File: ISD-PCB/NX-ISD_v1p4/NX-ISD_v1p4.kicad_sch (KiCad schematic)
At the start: 1 part

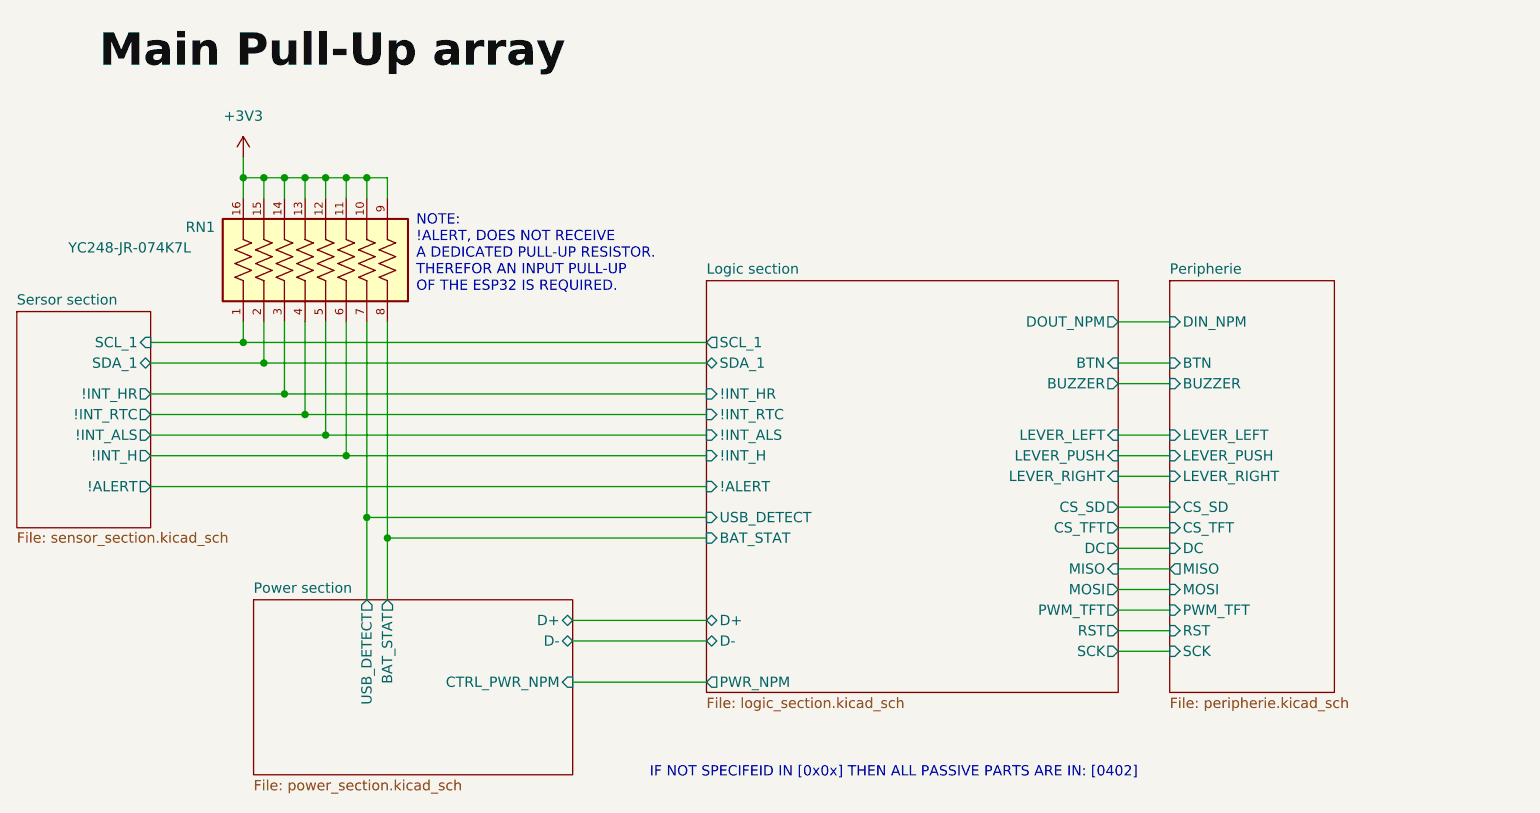
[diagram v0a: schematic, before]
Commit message: feat(pcb): v1.4 schematic and layout updates for 4-bit SDMMC, direct display SPI, and button pullups
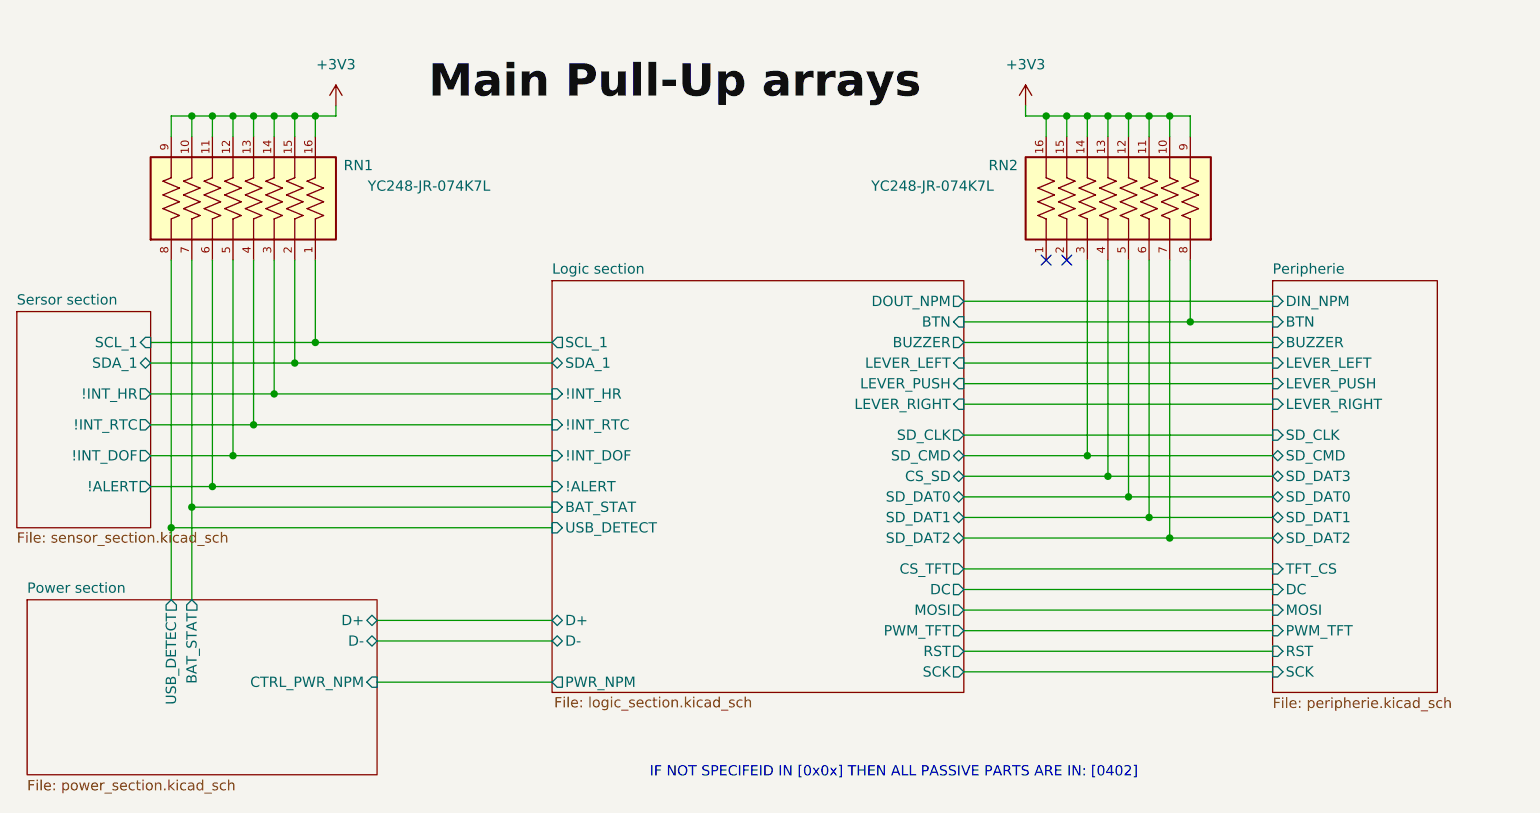
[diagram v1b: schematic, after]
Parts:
- added RN2: YC248-JR-074K7L, NX-AW-footprints:RESCAXS50P400X160X55-16N, symbol YC248-JR-074K7L:YC248-JR-074K7L
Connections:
- net Logic section/!INT_H is gone; now on net Logic section/!ALERT: RN1.6
- net +3V3: now also RN2.10, RN2.11, RN2.12, RN2.13, RN2.14, RN2.15, RN2.16, RN2.9
- net Logic section/BAT_STAT: now also RN1.7; no longer RN1.8
- net Logic section/BTN: now also RN2.8
- net Logic section/CS_SD: now also RN2.4
- net Logic section/USB_DETECT: now also RN1.8; no longer RN1.7
- net Logic section/!INT_ALS renamed Logic section/!INT_DOF
- new net Logic section/SD_CMD: RN2.3
- new net Logic section/SD_DAT0: RN2.5
- new net Logic section/SD_DAT1: RN2.6
- new net Logic section/SD_DAT2: RN2.7
- no-connect marks 0 -> 2
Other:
- sheet Logic section ports: added !INT_DOF, SD_CLK, SD_CMD, SD_DAT0, SD_DAT1, SD_DAT2; removed !INT_ALS, !INT_H, MISO
- sheet Peripherie ports: added SD_CLK, SD_CMD, SD_DAT0, SD_DAT1, SD_DAT2, SD_DAT3, TFT_CS; removed CS_SD, CS_TFT, MISO
- sheet Sersor section ports: added !INT_DOF; removed !INT_ALS, !INT_H
- note removed: "NOTE: !ALERT, DOES NOT RECEIVE A DEDICATED PULL-UP RESISTOR. THEREFOR AN INPUT PULL-UP OF THE ESP32 IS REQUIRED."

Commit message: hw(v1.4): relocate MicroSD to right edge and re-route BNO085 cluster; update READMEs
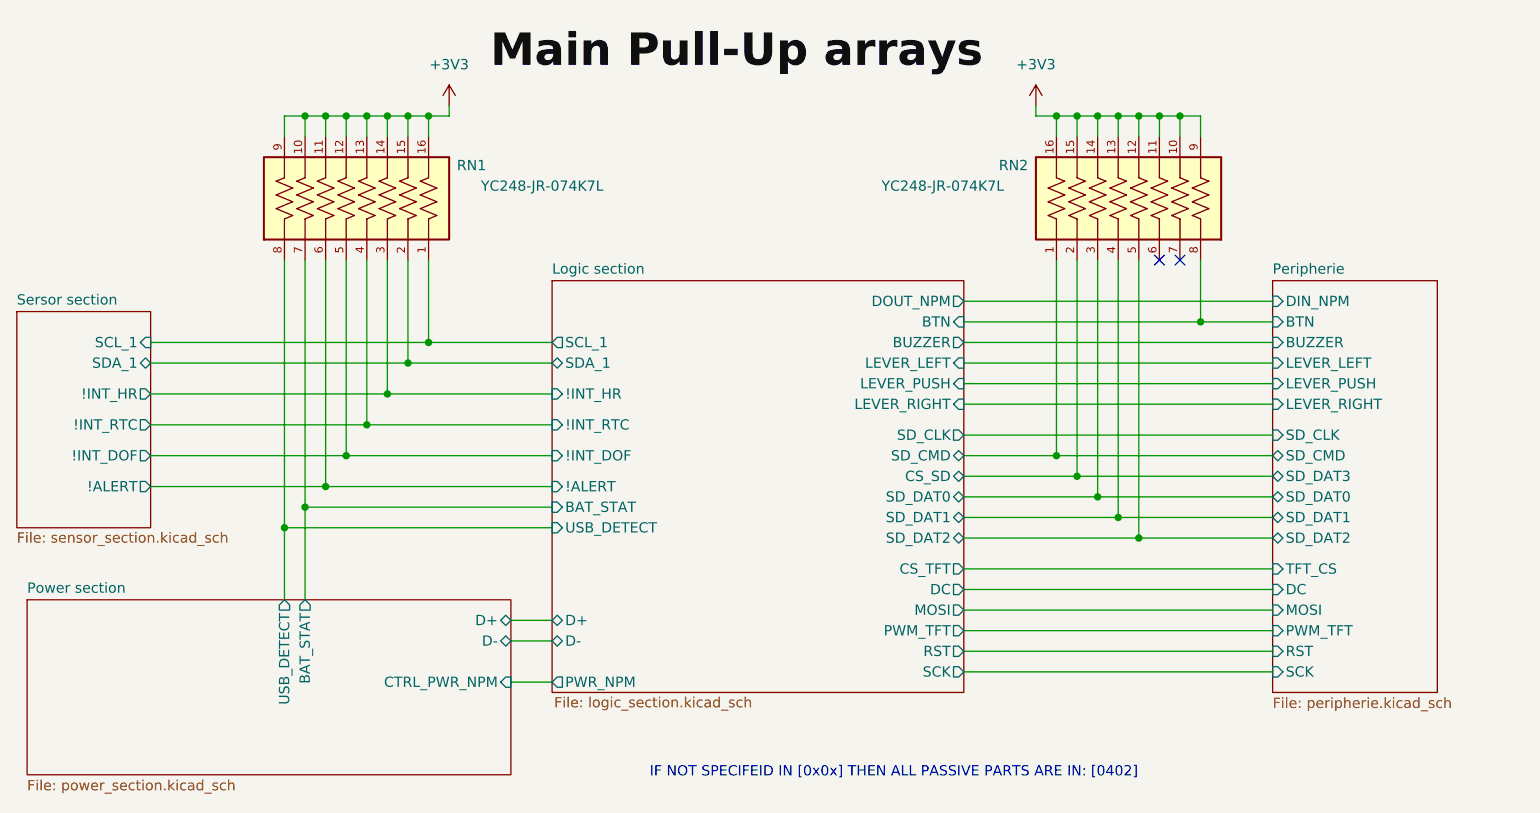
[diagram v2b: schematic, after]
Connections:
- net Logic section/CS_SD: now also RN2.2; no longer RN2.4
- net Logic section/SD_CMD: now also RN2.1; no longer RN2.3
- net Logic section/SD_DAT0: now also RN2.3; no longer RN2.5
- net Logic section/SD_DAT1: now also RN2.4; no longer RN2.6
- net Logic section/SD_DAT2: now also RN2.5; no longer RN2.7
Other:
- moved on the sheet: RN1

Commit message: hw(v1.4): progress on TODO - 4-bit MicroSD, direct display bus, BNO085 & EP vias (DRC 0 errors)
- Implemented 4-bit SDMMC MicroSD slot (Molex 105162-0001) on right edge with outward insertion
- Routed direct 3.3V display SPI bus (TE 1-2328702-0) with C29 100nF decoupling
- Centered BNO085 9-DOF IMU cluster with local ground star and 32.768kHz crystal
- Rerouted NeoPixel PWR_NPM high-side power gate signal
- Updated thermal EP pad via sizes on BQ25170 and MAX17048 for standard JLCPCB fabrication
- Achieved 0 DRC errors, 0 unconnected nets, and 100% schematic parity
- Updated HW-TODO and SW-TODO for v1.3/v1.4 pinout target abstraction
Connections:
- net Logic section/BAT_STAT: now also RN1.8; no longer RN1.7
- net Logic section/SD_CMD: now also RN2.3; no longer RN2.1
- net Logic section/SD_DAT0: now also RN2.4; no longer RN2.3
- net Logic section/SD_DAT1: now also RN2.5; no longer RN2.4
- net Logic section/SD_DAT2: now also RN2.1; no longer RN2.5
- net Logic section/USB_DETECT: now also RN1.7; no longer RN1.8

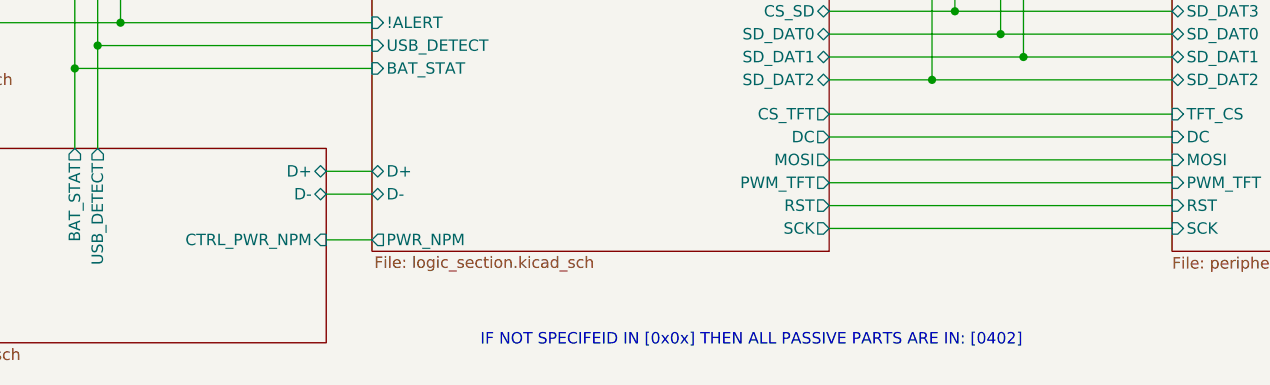
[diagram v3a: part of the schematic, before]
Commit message: hw(v1.4): bq25170 thermal optimization, usb-c plating, battery pad stitching, and npm decoupling
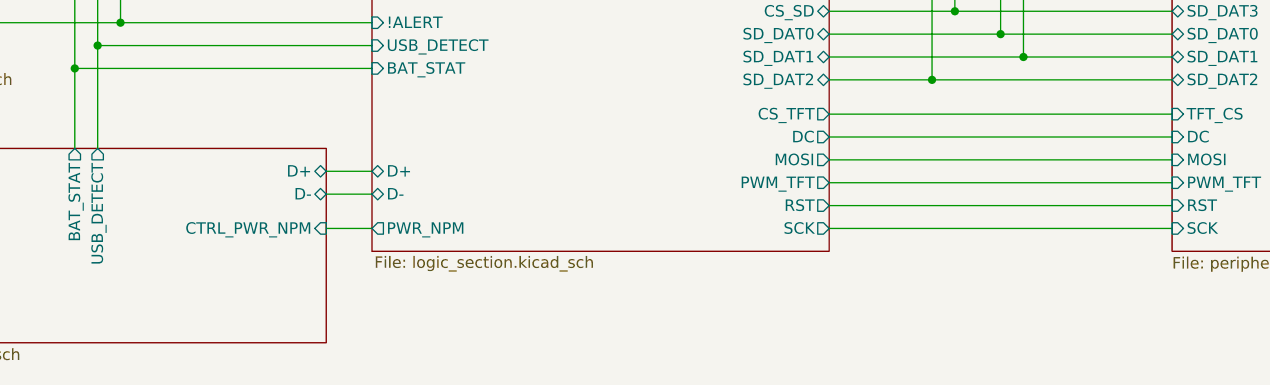
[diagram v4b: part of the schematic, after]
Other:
- note removed: "IF NOT SPECIFEID IN [0x0x] THEN ALL PASSIVE PARTS ARE IN: [0402]"
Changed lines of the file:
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@@
 		(date "2026-10-16")
 		(rev "p4")
-	)
-	(text "IF NOT SPECIFEID IN [0x0x] THEN ALL PASSIVE PARTS ARE IN: [0402]"
-		(exclude_from_sim no)
-		(at 124.714 106.426 0)
-		(effects
-			(font
-				(size 1.27 1.27)
-			)
-		)
+		(comment 1 "IF NOT SPECIFID IN [0x0x] THEN ALL PASSIVE PARTS ARE IN: [0402]")
 	)
 	(junction
@@
 	(wire
 		(pts
-			(xy 77.47 95.25) (xy 82.55 95.25)
+			(xy 77.47 93.98) (xy 82.55 93.98)
 		)
 		(stroke
@@
 		)
 		(pin "CTRL_PWR_NPM" input
-			(at 77.47 95.25 0)
+			(at 77.47 93.98 0)
 			(effects
 				(font
@@
 		)
 		(pin "PWR_NPM" output
-			(at 82.55 95.25 180)
-			(effects
-				(font
+			(at 82.55 93.98 180)
+			(effects
+				(font

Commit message: hw(v1p4): add RTC backup supercap C27, tactile buttons, USBLC6 footprint adjustments, and cyberpunk silkscreens
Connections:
- net Logic section/BTN: now also RN2.1; no longer RN2.8
- net Logic section/CS_SD: now also RN2.4; no longer RN2.2
- net Logic section/SD_CMD: now also RN2.5; no longer RN2.3
- net Logic section/SD_DAT0: now also RN2.6; no longer RN2.4
- net Logic section/SD_DAT1: now also RN2.7; no longer RN2.5
- net Logic section/SD_DAT2: now also RN2.3; no longer RN2.1
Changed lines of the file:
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@@
+	)
+	(junction
+		(at 144.78 50.8)
+		(diameter 0)
+		(color 0 0 0 0)
 	)
 	(junction
@@
 	)
 	(junction
-		(at 154.94 74.93)
-		(diameter 0)
-		(color 0 0 0 0)
-	)
-	(junction
-		(at 144.78 77.47)
-		(diameter 0)
-		(color 0 0 0 0)
-	)
-	(junction
-		(at 149.86 67.31)
+		(at 160.02 74.93)
 		(diameter 0)
 		(color 0 0 0 0)
@@
 	)
 	(junction
+		(at 152.4 69.85)
+		(diameter 0)
+		(color 0 0 0 0)
+	)
+	(junction
 		(at 67.31 53.34)
 		(diameter 0)
@@
 	)
 	(junction
-		(at 152.4 72.39)
-		(diameter 0)
-		(color 0 0 0 0)
-	)
-	(junction
-		(at 147.32 69.85)
+		(at 154.94 67.31)
 		(diameter 0)
 		(color 0 0 0 0)
@@
 	)
 	(junction
+		(at 157.48 72.39)
+		(diameter 0)
+		(color 0 0 0 0)
+	)
+	(junction
 		(at 160.02 25.4)
 		(diameter 0)
@@
 	)
 	(junction
+		(at 149.86 77.47)
+		(diameter 0)
+		(color 0 0 0 0)
+	)
+	(junction
 		(at 157.48 25.4)
 		(diameter 0)
@@
 	)
 	(junction
-		(at 162.56 50.8)
-		(diameter 0)
-		(color 0 0 0 0)
-	)
-	(junction
 		(at 64.77 25.4)
 		(diameter 0)
@@
 	)
 	(no_connect
-		(at 157.48 43.18)
+		(at 162.56 43.18)
 	)
 	(no_connect
-		(at 160.02 43.18)
+		(at 147.32 43.18)
+	)
+	(wire
+		(pts
+			(xy 154.94 67.31) (xy 171.45 67.31)
+		)
+		(stroke
+			(width 0)
+			(type default)
+		)
 	)
 	(wire
@@
 	(wire
 		(pts
-			(xy 149.86 43.18) (xy 149.86 67.31)
+			(xy 149.86 77.47) (xy 171.45 77.47)
 		)
 		(stroke
@@
 	(wire
 		(pts
-			(xy 133.35 72.39) (xy 152.4 72.39)
+			(xy 152.4 69.85) (xy 171.45 69.85)
 		)
 		(stroke
@@
 	(wire
 		(pts
-			(xy 133.35 69.85) (xy 147.32 69.85)
-		)
-		(stroke
-			(width 0)
-			(type default)
-		)
-	)
-	(wire
-		(pts
 			(xy 133.35 64.77) (xy 171.45 64.77)
 		)
@@
 	(wire
 		(pts
-			(xy 162.56 50.8) (xy 171.45 50.8)
+			(xy 133.35 50.8) (xy 144.78 50.8)
+		)
+		(stroke
+			(width 0)
+			(type default)
+		)
+	)
+	(wire
+		(pts
+			(xy 144.78 50.8) (xy 171.45 50.8)
 		)
 		(stroke
@@
 	(wire
 		(pts
-			(xy 154.94 43.18) (xy 154.94 74.93)
-		)
-		(stroke
-			(width 0)
-			(type default)
-		)
-	)
-	(wire
-		(pts
 			(xy 77.47 90.17) (xy 82.55 90.17)
 		)
@@
 	(wire
 		(pts
-			(xy 133.35 77.47) (xy 144.78 77.47)
-		)
-		(stroke
-			(width 0)
-			(type default)
-		)
-	)
-	(wire
-		(pts
 			(xy 133.35 88.9) (xy 171.45 88.9)
 		)
@@
 	(wire
 		(pts
+			(xy 160.02 74.93) (xy 171.45 74.93)
+		)
+		(stroke
+			(width 0)
+			(type default)
+		)
+	)
+	(wire
+		(pts
 			(xy 33.02 53.34) (xy 67.31 53.34)
 		)
@@
 	(wire
 		(pts
-			(xy 133.35 74.93) (xy 154.94 74.93)
+			(xy 133.35 74.93) (xy 160.02 74.93)
 		)
 		(stroke
@@
 	(wire
 		(pts
-			(xy 154.94 74.93) (xy 171.45 74.93)
+			(xy 160.02 43.18) (xy 160.02 74.93)
 		)
 		(stroke
@@
 	(wire
 		(pts
-			(xy 162.56 43.18) (xy 162.56 50.8)
-		)
-		(stroke
-			(width 0)
-			(type default)
-		)
-	)
-	(wire
-		(pts
 			(xy 52.07 73.66) (xy 82.55 73.66)
 		)
@@
 	(wire
 		(pts
+			(xy 149.86 43.18) (xy 149.86 77.47)
+		)
+		(stroke
+			(width 0)
+			(type default)
+		)
+	)
+	(wire
+		(pts
 			(xy 49.53 43.18) (xy 49.53 76.2)
 		)
@@
 	(wire
 		(pts
-			(xy 149.86 67.31) (xy 171.45 67.31)
+			(xy 133.35 67.31) (xy 154.94 67.31)
 		)
 		(stroke
@@
 	(wire
 		(pts
+			(xy 157.48 72.39) (xy 171.45 72.39)
+		)
+		(stroke
+			(width 0)
+			(type default)
+		)
+	)
+	(wire
+		(pts
 			(xy 162.56 25.4) (xy 162.56 27.94)
 		)
@@
 	(wire
 		(pts
-			(xy 133.35 67.31) (xy 149.86 67.31)
-		)
-		(stroke
-			(width 0)
-			(type default)
-		)
-	)
-	(wire
-		(pts
 			(xy 49.53 25.4) (xy 49.53 27.94)
 		)
@@
 	(wire
 		(pts
-			(xy 152.4 72.39) (xy 171.45 72.39)
-		)
-		(stroke
-			(width 0)
-			(type default)
-		)
-	)
-	(wire
-		(pts
-			(xy 147.32 43.18) (xy 147.32 69.85)
-		)
-		(stroke
-			(width 0)
-			(type default)
-		)
-	)
-	(wire
-		(pts
-			(xy 152.4 43.18) (xy 152.4 72.39)
+			(xy 133.35 72.39) (xy 157.48 72.39)
+		)
+		(stroke
+			(width 0)
+			(type default)
+		)
+	)
+	(wire
+		(pts
+			(xy 157.48 43.18) (xy 157.48 72.39)
+		)
+		(stroke
+			(width 0)
+			(type default)
+		)
+	)
+	(wire
+		(pts
+			(xy 154.94 43.18) (xy 154.94 67.31)
+		)
+		(stroke
+			(width 0)
+			(type default)
+		)
+	)
+	(wire
+		(pts
+			(xy 144.78 43.18) (xy 144.78 50.8)
 		)
 		(stroke
@@
 	(wire
 		(pts
+			(xy 152.4 43.18) (xy 152.4 69.85)
+		)
+		(stroke
+			(width 0)
+			(type default)
+		)
+	)
+	(wire
+		(pts
 			(xy 54.61 71.12) (xy 82.55 71.12)
 		)
@@
 	(wire
 		(pts
-			(xy 144.78 77.47) (xy 171.45 77.47)
-		)
-		(stroke
-			(width 0)
-			(type default)
-		)
-	)
-	(wire
-		(pts
-			(xy 144.78 43.18) (xy 144.78 77.47)
+			(xy 133.35 77.47) (xy 149.86 77.47)
 		)
 		(stroke
@@
 	(wire
 		(pts
-			(xy 133.35 50.8) (xy 162.56 50.8)
-		)
-		(stroke
-			(width 0)
-			(type default)
-		)
-	)
-	(wire
-		(pts
-			(xy 147.32 69.85) (xy 171.45 69.85)
-		)
-		(stroke
+			(xy 133.35 69.85) (xy 152.4 69.85)
+		)
+		(stroke
